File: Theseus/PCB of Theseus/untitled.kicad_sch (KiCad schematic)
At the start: 30 parts, among them J1 Conn_01x06_Socket, J2 Conn_01x06_Socket, J4 Conn_01x06_Socket, J8 Conn_01x06_Socket, Q1 DMG1012UW-7, Q2 DMG1012UW-7, U13 MAX6675

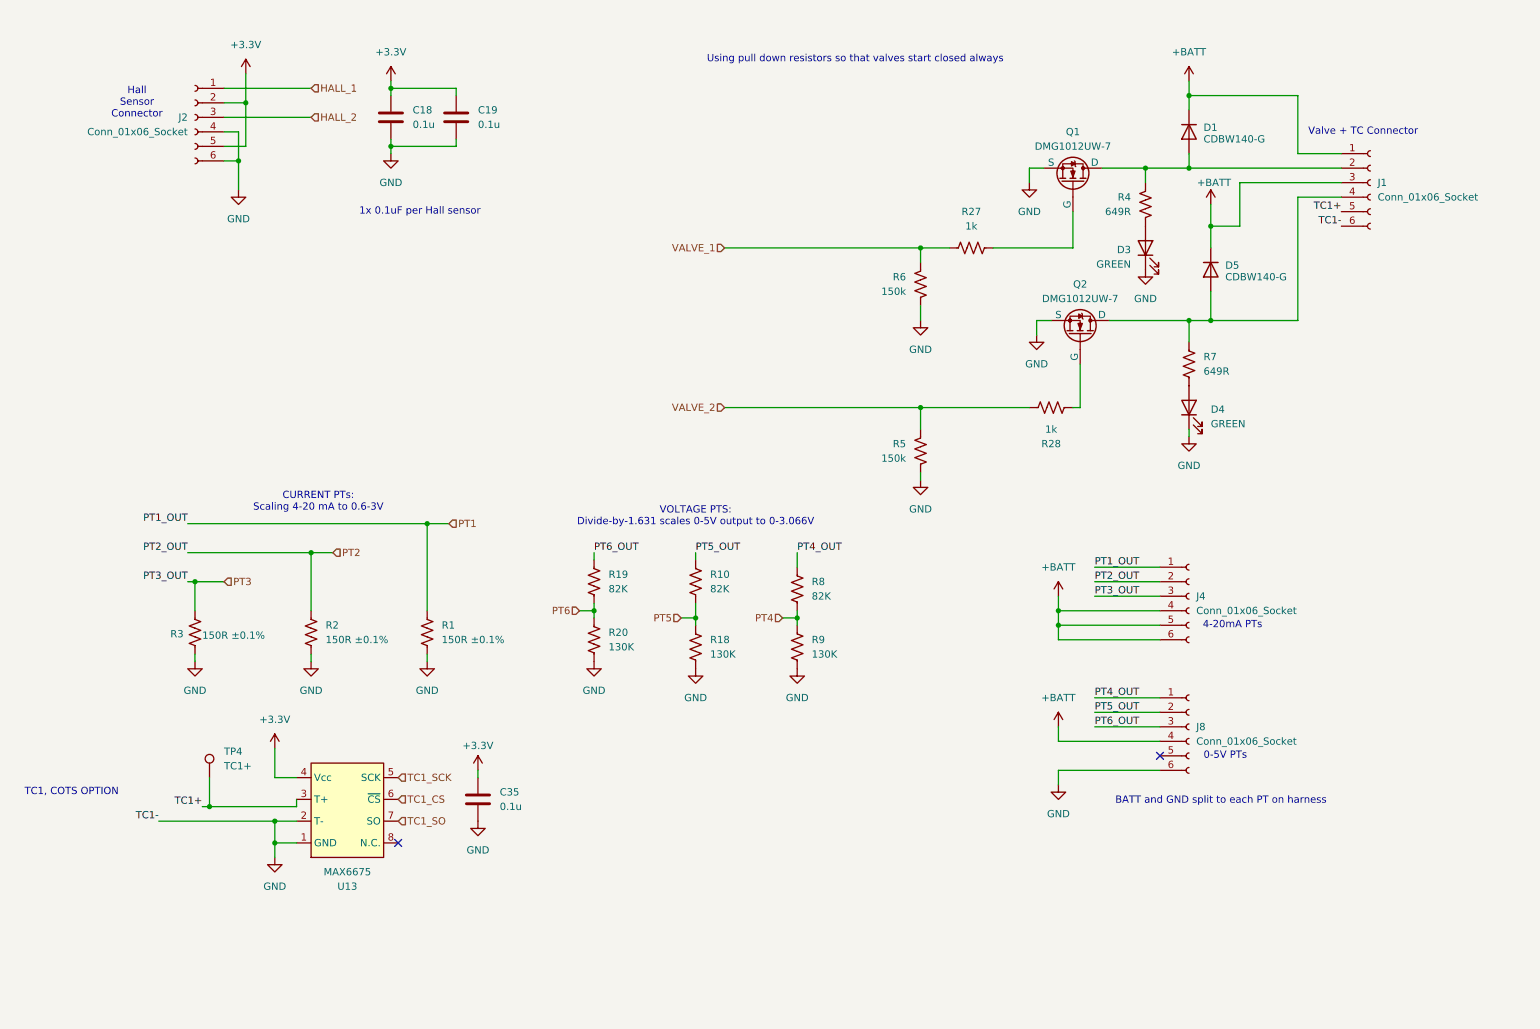
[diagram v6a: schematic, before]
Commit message: layout and routing + minor schematic changes
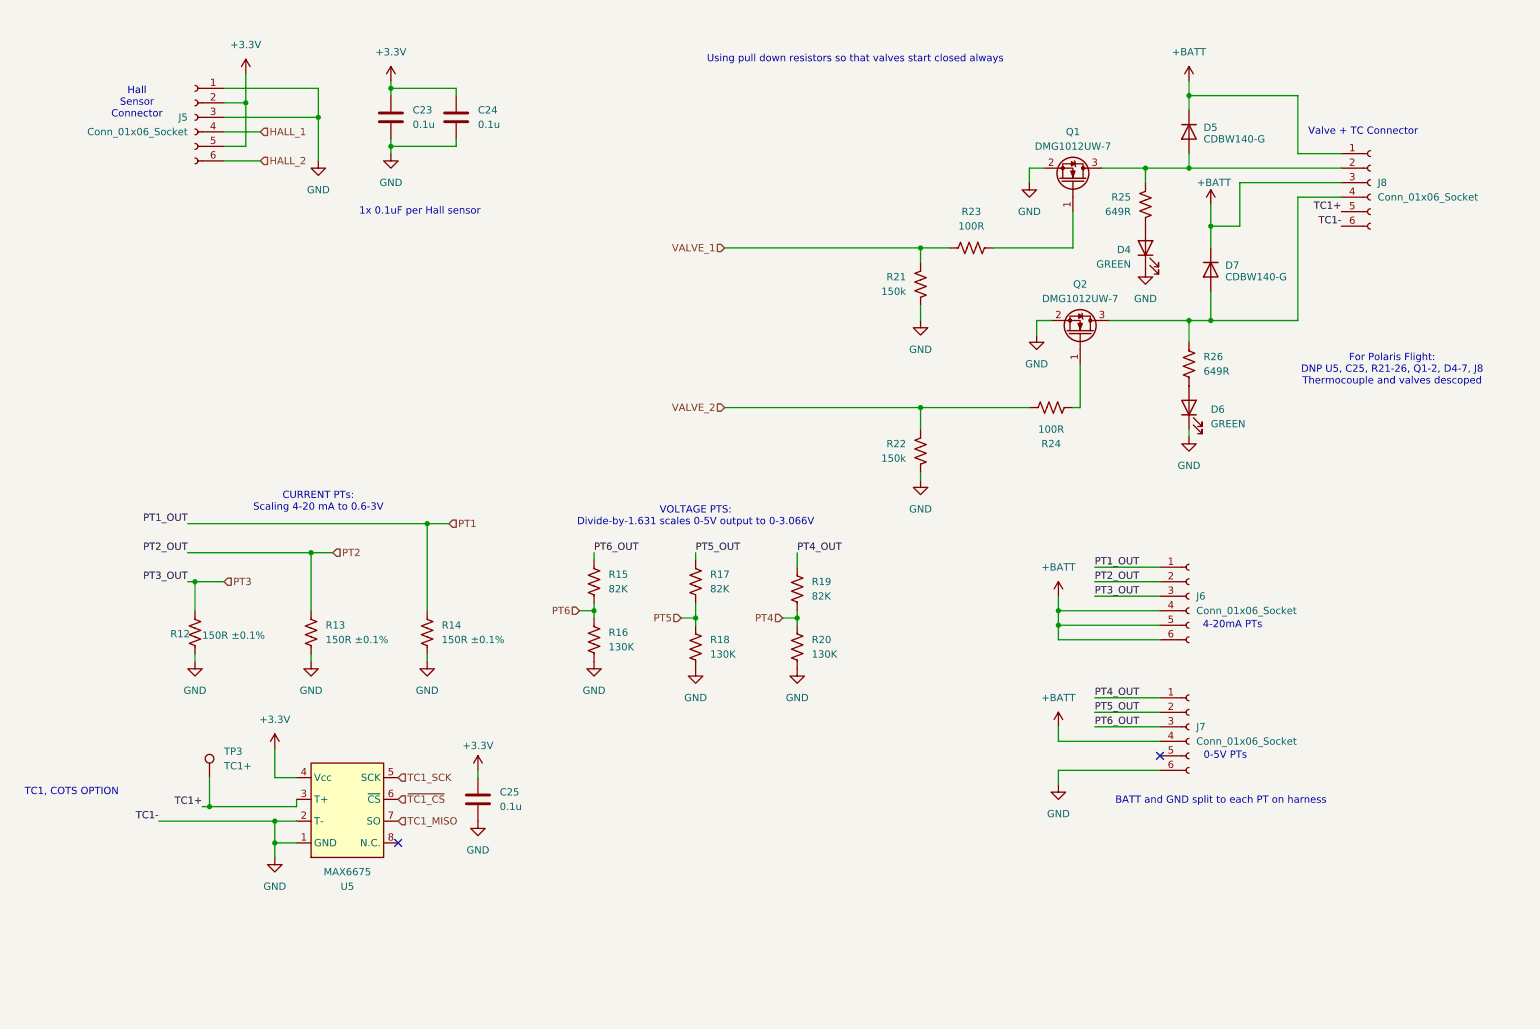
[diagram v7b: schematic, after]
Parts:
- removed J4, J8: Conn_01x06_Socket, canhw_footprints:connector_Harwin_G125–MG10605M4P, symbol Connector:Conn_01x06_Socket
- removed Q2: DMG1012UW-7, Package_TO_SOT_SMD:SOT-323_SC-70_Handsoldering, symbol Simulation_SPICE:NMOS
- added J6, J7: Conn_01x06_Socket, canhw_footprints:connector_Harwin_G125–MG10605M4P, symbol Connector:Conn_01x06_Socket
- added Q2: DMG1012UW-7, Fydp_footprints:SOT_12UW-7_DIO, symbol Transistor_FET_Other:Q_NMOS_Depletion_GSD
- D4: renamed from D3; footprint Diode_SMD:D_0603_1608Metric_Pad1.05x0.95mm_HandSolder -> LED_SMD:LED_1206_3216Metric_Pad1.42x1.75mm_HandSolder
- D6: renamed from D4; footprint Diode_SMD:D_0603_1608Metric_Pad1.05x0.95mm_HandSolder -> LED_SMD:LED_1206_3216Metric_Pad1.42x1.75mm_HandSolder
- Q1: footprint Package_TO_SOT_SMD:SOT-323_SC-70_Handsoldering -> Fydp_footprints:SOT_12UW-7_DIO; symbol Simulation_SPICE:NMOS -> Transistor_FET_Other:Q_NMOS_Depletion_GSD
- R23: renamed from R27; value 1k -> 100R
- R24: renamed from R28; value 1k -> 100R
- renumbered C18 to C23, C19 to C24, C35 to C25, D1 to D5, D5 to D7, J2 to J5, J1 to J8, R3 to R12, R2 to R13, R1 to R14, R19 to R15, R20 to R16, R10 to R17, R8 to R19, R9 to R20, R6 to R21, R5 to R22, R4 to R25, R7 to R26, TP4 to TP3, U13 to U5
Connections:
- net +BATT: now also J6.4 (Pin_4), J6.5 (Pin_5), J6.6 (Pin_6), J7.4 (Pin_4)
- net GND: now also J5.1 (Pin_1), J5.3 (Pin_3), Q1.2 (S), J7.6 (Pin_6), Q2.2 (S); no longer J5.4 (Pin_4), J5.6 (Pin_6), Q1.3 (S)
- net HALL_1: now also J5.4 (Pin_4); no longer J5.1 (Pin_1)
- net HALL_2: now also J5.6 (Pin_6); no longer J5.3 (Pin_3)
- net PT1: now also J6.1 (Pin_1)
- net PT2: now also J6.2 (Pin_2)
- net PT3: now also J6.3 (Pin_3)
- net PT4_OUT: now also J7.1 (Pin_1)
- net PT5_OUT: now also J7.2 (Pin_2)
- net PT6_OUT: now also J7.3 (Pin_3)
- net at D5.2 (A), J8.2 (Pin_2), R25.2: now also Q1.3 (D); no longer Q1.1 (D)
- net at R23.1: now also Q1.1 (G); no longer Q1.2 (G)
- net at D7.2 (A), J8.4 (Pin_4), R26.1: now also Q2.3 (D)
- net at R24.1: now also Q2.1 (G)
- net TC1_CS renamed ~{TC1_CS}
- net TC1_SO renamed TC1_MISO
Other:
- note added: "For Polaris Flight: DNP U5, C25, R21-26, Q1-2, D4-7, J8 Thermocouple and valves descoped"
